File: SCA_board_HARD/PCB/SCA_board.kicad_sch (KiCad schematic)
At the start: 44 parts, among them IC1 ST3232BDR, J1 100616-2, J2 39-29-3086, J3 DIN41612_02x32_AC, J4 USB4145-03-0230-C, J5 DE9_Pins, J6 USB4145-03-0230-C, J7 Conn_01x03, U1 USBLC6-2SC6, U2 CH340E

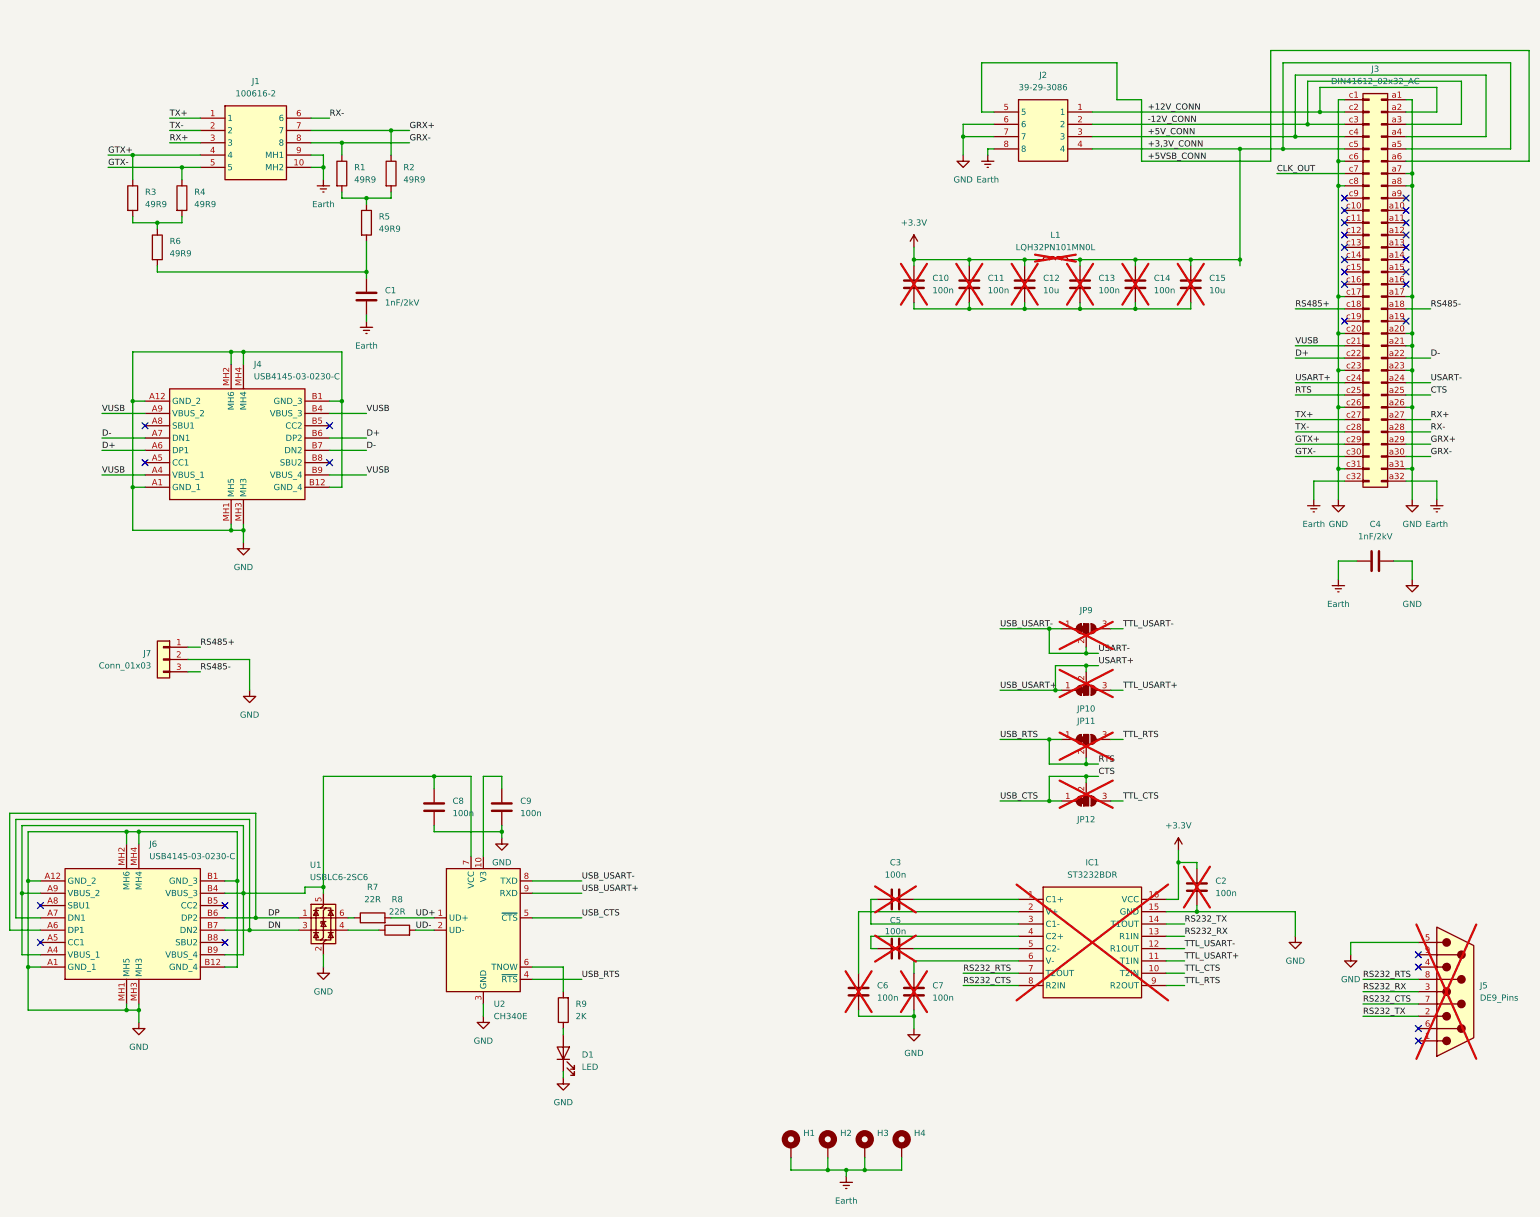
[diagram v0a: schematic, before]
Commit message: Added i2c config eeprom and testpoints
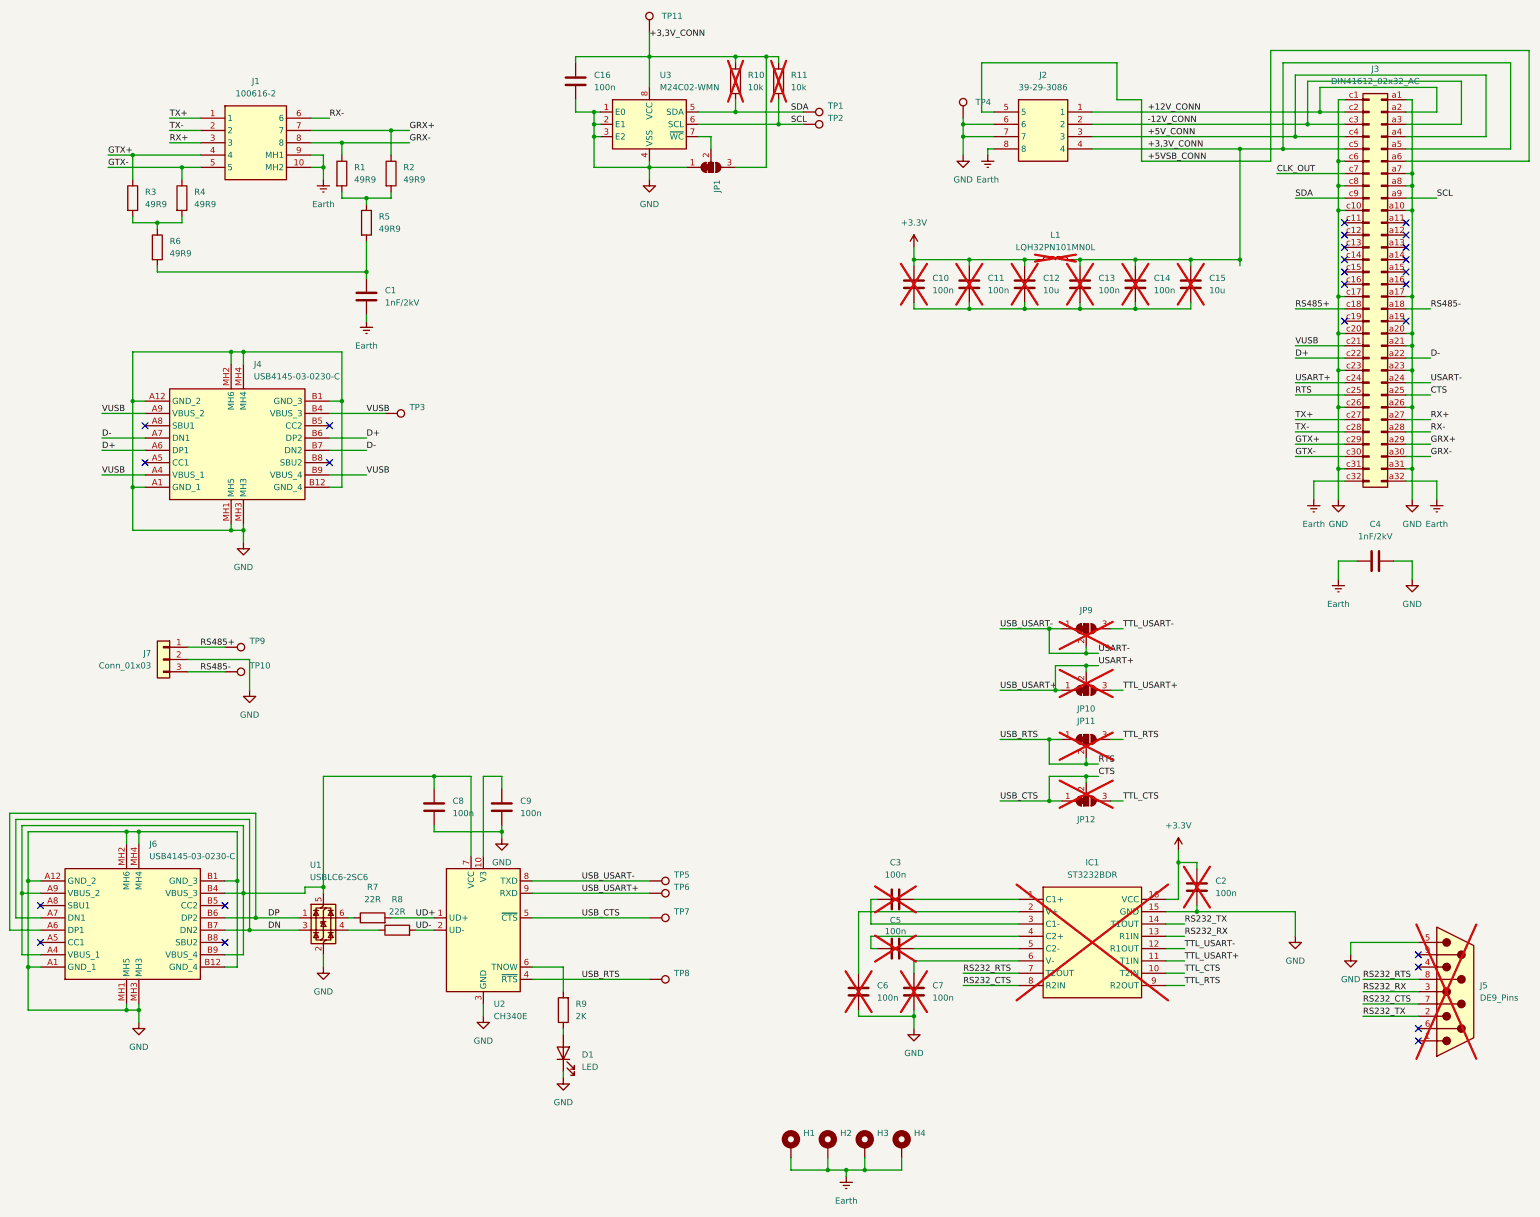
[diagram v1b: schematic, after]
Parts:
- added C16: 100n, Capacitor_SMD:C_0603_1608Metric_Pad1.08x0.95mm_HandSolder, symbol Device:C
- added JP1: SolderJumper_3_Bridged12, Jumper:SolderJumper-3_P1.3mm_Bridged12_Pad1.0x1.5mm, symbol Jumper:SolderJumper_3_Bridged12
- added R10, R11: 10k, Resistor_SMD:R_0603_1608Metric_Pad0.98x0.95mm_HandSolder, symbol Device:R
- added TP1, TP10, TP11, TP2, TP3, TP4, TP5, TP6, TP7, TP8, TP9: TestPoint, TestPoint:TestPoint_Pad_D1.0mm, symbol Connector:TestPoint
- added U3: M24C02-WMN, Package_SO:SOIC-8_3.9x4.9mm_P1.27mm, symbol Memory_EEPROM:M24C02-WMN
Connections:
- net +3,3V_CONN: now also C16.2, JP1.3 (B), R10.2, R11.2, TP11.1, U3.8 (VCC)
- net CTS: now also TP7.1
- net GND: now also J3.a10 (Pin_a10), J3.c10 (Pin_c10), C16.1, JP1.1 (A), TP4.1, U3.1 (E0), U3.2 (E1), U3.3 (E2), U3.4 (VSS)
- net RS485+: now also TP9.1
- net RS485-: now also TP10.1
- net RTS: now also TP8.1
- net USART+: now also TP6.1
- net USART-: now also TP5.1
- net VUSB: now also TP3.1
- net SCL: now reaches J3.a9 (Pin_a9)
- net SCL: now also R11.1, TP2.1, U3.6 (SCL)
- net SDA: now reaches J3.c9 (Pin_c9)
- net SDA: now also R10.1, TP1.1, U3.5 (SDA)
- new net: JP1.2 (C), U3.7 (~{WC})
- no-connect marks 30 -> 26
